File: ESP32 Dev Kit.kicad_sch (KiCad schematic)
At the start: 22 parts, among them J1 USB_B_Micro, Q1 2N2222, Q2 2N2222, SW1 SW_Push, SW2 SW_Push, U1 AMS1117-3.3, U2 CH340C

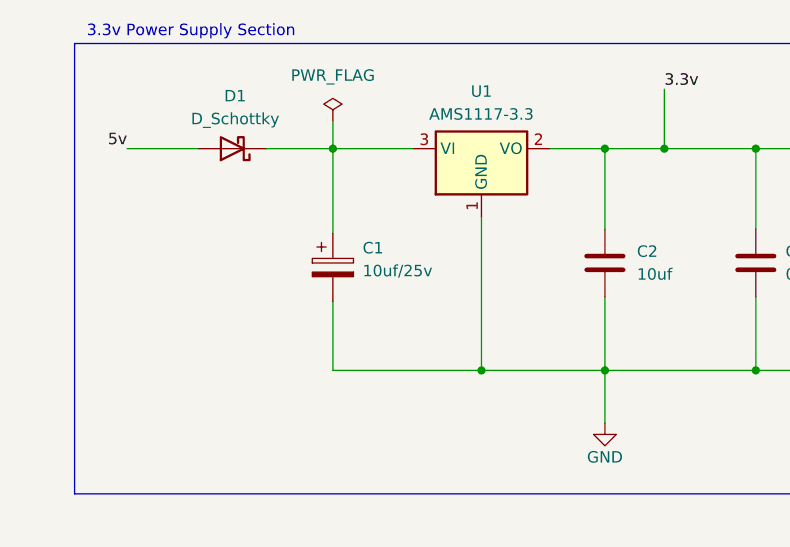
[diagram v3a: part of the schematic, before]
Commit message: Added Footprints to the Symbols
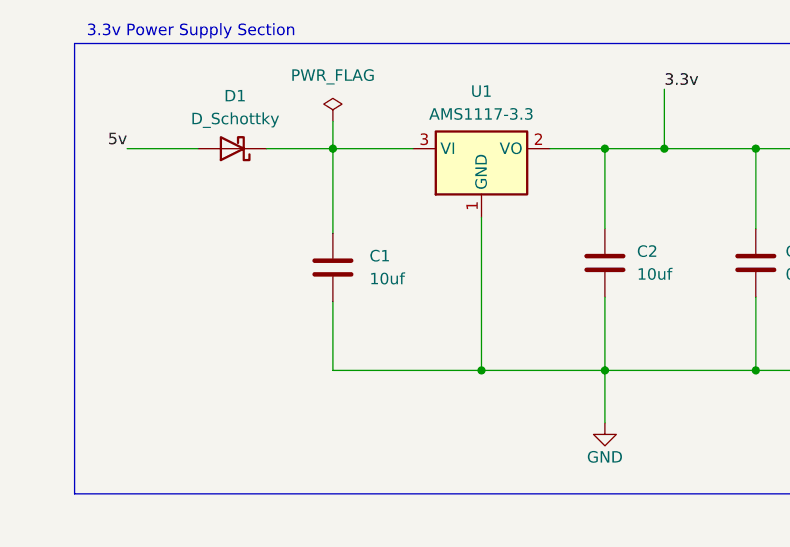
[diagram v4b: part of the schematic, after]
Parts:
- removed C1: 10uf/25v, symbol Device:C_Polarized
- added C1: 10uf, Capacitor_SMD:C_0805_2012Metric_Pad1.18x1.45mm_HandSolder, symbol Device:C
- C2, C3, C4, C5, C6: footprint (none) -> Capacitor_SMD:C_0805_2012Metric_Pad1.18x1.45mm_HandSolder
- D1: footprint (none) -> Diode_SMD:D_SOD-123
- D2: footprint (none) -> LED_SMD:LED_0805_2012Metric_Pad1.15x1.40mm_HandSolder
- J1: footprint (none) -> Connector_USB:USB_Micro-B_Molex_47346-0001
- R1, R2, R3, R4, R5, R6: footprint (none) -> Resistor_SMD:R_0805_2012Metric_Pad1.20x1.40mm_HandSolder
- SW1, SW2: footprint (none) -> Button_Switch_SMD:SW_SPST_B3U-1000P
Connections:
- net GND: now also C1.2
- net at D1.1 (K), U1.3 (VI): now also C1.1
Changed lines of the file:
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@@
 			)
 		)
-		(property "Footprint" ""
+		(property "Footprint" "Capacitor_SMD:C_0805_2012Metric_Pad1.18x1.45mm_HandSolder"
 			(at 220.218 70.6628 0)
 			(effects
@@
 			)
 		)
-		(property "Footprint" ""
+		(property "Footprint" "Connector_USB:USB_Micro-B_Molex_47346-0001"
 			(at 190.754 121.666 0)
 			(effects
@@
 			)
 		)
-		(property "Footprint" ""
+		(property "Footprint" "Resistor_SMD:R_0805_2012Metric_Pad1.20x1.40mm_HandSolder"
 			(at 114.808 41.148 90)
 			(effects
@@
 			)
 		)
-		(property "Footprint" ""
+		(property "Footprint" "Diode_SMD:D_SOD-123"
 			(at 48.26 39.37 0)
 			(effects
@@
 			)
 		)
-		(property "Footprint" ""
+		(property "Footprint" "Capacitor_SMD:C_0805_2012Metric_Pad1.18x1.45mm_HandSolder"
 			(at 177.4952 141.224 0)
 			(effects
@@
 			)
 		)
-		(property "Footprint" ""
+		(property "Footprint" "Resistor_SMD:R_0805_2012Metric_Pad1.20x1.40mm_HandSolder"
 			(at 171.704 44.958 90)
 			(effects
@@
 			)
 		)
-		(property "Footprint" ""
+		(property "Footprint" "Capacitor_SMD:C_0805_2012Metric_Pad1.18x1.45mm_HandSolder"
 			(at 107.3912 55.88 0)
 			(effects
@@
 			)
 		)
-		(property "Footprint" ""
+		(property "Footprint" "Resistor_SMD:R_0805_2012Metric_Pad1.20x1.40mm_HandSolder"
 			(at 182.626 137.668 90)
 			(effects
@@
 			)
 		)
-		(property "Footprint" ""
+		(property "Footprint" "Capacitor_SMD:C_0805_2012Metric_Pad1.18x1.45mm_HandSolder"
 			(at 90.6272 55.88 0)
 			(effects
@@
 			)
 		)
-		(property "Footprint" ""
+		(property "Footprint" "Button_Switch_SMD:SW_SPST_B3U-1000P"
 			(at 192.532 38.1 0)
 			(effects
@@
 			)
 		)
-		(property "Footprint" ""
+		(property "Footprint" "Button_Switch_SMD:SW_SPST_B3U-1000P"
 			(at 250.444 37.846 0)
 			(effects
@@
 			)
 		)
-		(property "Footprint" ""
+		(property "Footprint" "Capacitor_SMD:C_0805_2012Metric_Pad1.18x1.45mm_HandSolder"
 			(at 215.0872 110.744 0)
 			(effects
@@
 	)
 	(symbol
-		(lib_id "Device:C_Polarized")
+		(lib_id "Device:C")
 		(at 59.436 52.578 0)
 		(unit 1)
@@
 		(fields_autoplaced yes)
 		(property "Reference" "C1"
-			(at 62.738 50.4189 0)
-			(effects
-				(font
-					(size 1.27 1.27)
-				)
-				(justify left)
-			)
-		)
-		(property "Value" "10uf/25v"
-			(at 62.738 52.9589 0)
-			(effects
-				(font
-					(size 1.27 1.27)
-				)
-				(justify left)
-			)
-		)
-		(property "Footprint" ""
+			(at 63.5 51.3079 0)
+			(effects
+				(font
+					(size 1.27 1.27)
+				)
+				(justify left)
+			)
+		)
+		(property "Value" "10uf"
+			(at 63.5 53.8479 0)
+			(effects
+				(font
+					(size 1.27 1.27)
+				)
+				(justify left)
+			)
+		)
+		(property "Footprint" "Capacitor_SMD:C_0805_2012Metric_Pad1.18x1.45mm_HandSolder"
 			(at 60.4012 56.388 0)
 			(effects
@@
 			)
 		)
-		(property "Description" "Polarized capacitor"
+		(property "Description" "Unpolarized capacitor"
 			(at 59.436 52.578 0)
 			(effects
@@
 			)
 		)
-		(pin "1"
-		)
 		(pin "2"
 		)
-		(instances
-			(project ""
+		(pin "1"
+		)
+		(instances
+			(project "ESP32 Dev Kit"
 				(path "/56a9cdb5-133f-4918-8bc1-4c774ad33a13"
 					(reference "C1")
@@
 			)
 		)
-		(property "Footprint" ""
+		(property "Footprint" "Resistor_SMD:R_0805_2012Metric_Pad1.20x1.40mm_HandSolder"
 			(at 229.362 44.704 90)
 			(effects
@@
 			)
 		)
-		(property "Footprint" ""
+		(property "Footprint" "LED_SMD:LED_0805_2012Metric_Pad1.15x1.40mm_HandSolder"
 			(at 124.714 52.07 0)
 			(effects
@@
 			)
 		)
-		(property "Footprint" ""
+		(property "Footprint" "Resistor_SMD:R_0805_2012Metric_Pad1.20x1.40mm_HandSolder"
 			(at 257.302 54.864 90)
 			(effects
@@
 			)
 		)
-		(property "Footprint" ""
+		(property "Footprint" "Resistor_SMD:R_0805_2012Metric_Pad1.20x1.40mm_HandSolder"
 			(at 199.39 53.34 90)
 			(effects

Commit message: Schematic and Footprints Revised
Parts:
- removed MOD1: ESP32-WROOM-32, digikey-footprints:ESP32-WROOM-32D, symbol dk_RF-Transceiver-Modules:ESP32-WROOM-32
- added U3: ESP32-WROOM-32, RF_Module:ESP32-WROOM-32, symbol RF_Module:ESP32-WROOM-32
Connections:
- net 3.3v: now also U3.2 (VDD)
- net Boot: now also U3.25 (IO0)
- net D12: now also U3.14 (IO12)
- net D13: now also U3.16 (IO13)
- net D14: now also U3.13 (IO14)
- net D15: now also U3.23 (IO15)
- net D18: now also U3.30 (IO18)
- net D19: now also U3.31 (IO19)
- net D2: now also U3.24 (IO2)
- net D21: now also U3.33 (IO21)
- net D22: now also U3.36 (IO22)
- net D23: now also U3.37 (IO23)
- net D25: now also U3.10 (IO25)
- net D26: now also U3.11 (IO26)
- net D27: now also U3.12 (IO27)
- net D32: now also U3.8 (IO32)
- net D33: now also U3.9 (IO33)
- net D34: now also U3.6 (IO34)
- net D35: now also U3.7 (IO35)
- net D4: now also U3.26 (IO4)
- net D5: now also U3.29 (IO5)
- net EN: now also U3.3 (EN)
- net GND: now also U3.1 (GND), U3.15 (GND), U3.38 (GND), U3.39 (GND)
- net RX0: now also U3.34 (RXD0/IO3)
- net RX2: now also U3.27 (IO16)
- net TX0: now also U3.35 (TXD0/IO1)
- net TX2: now also U3.28 (IO17)
- net VN: now also U3.5 (SENSOR_VN)
- net VP: now also U3.4 (SENSOR_VP)

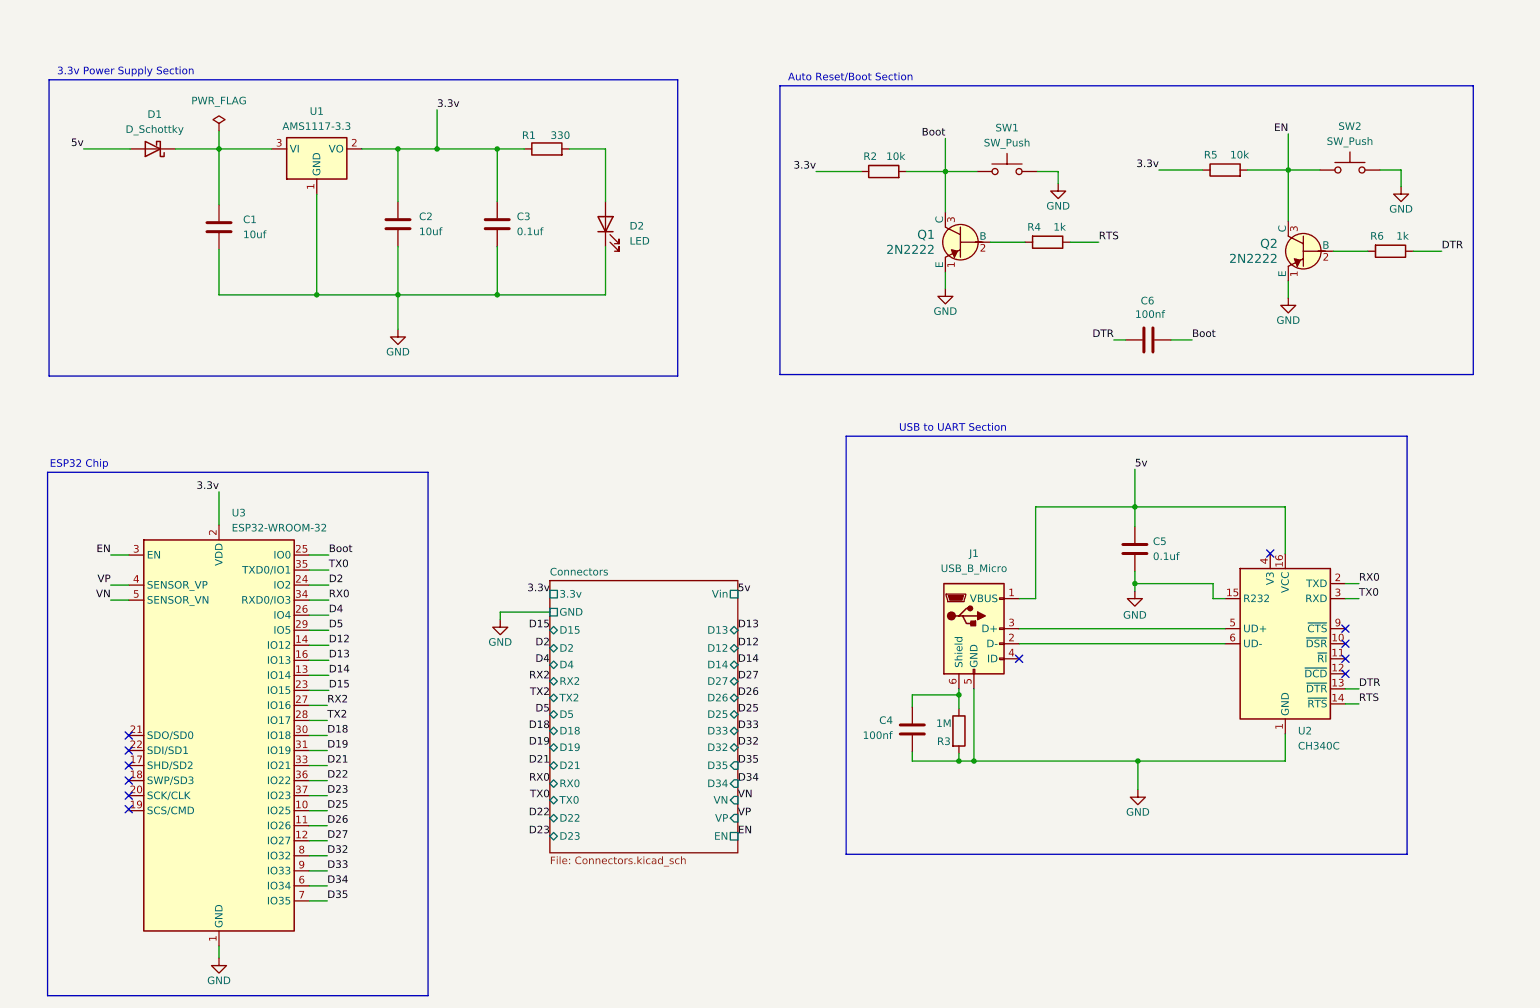
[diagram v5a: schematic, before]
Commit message: Footprints placed & Revised
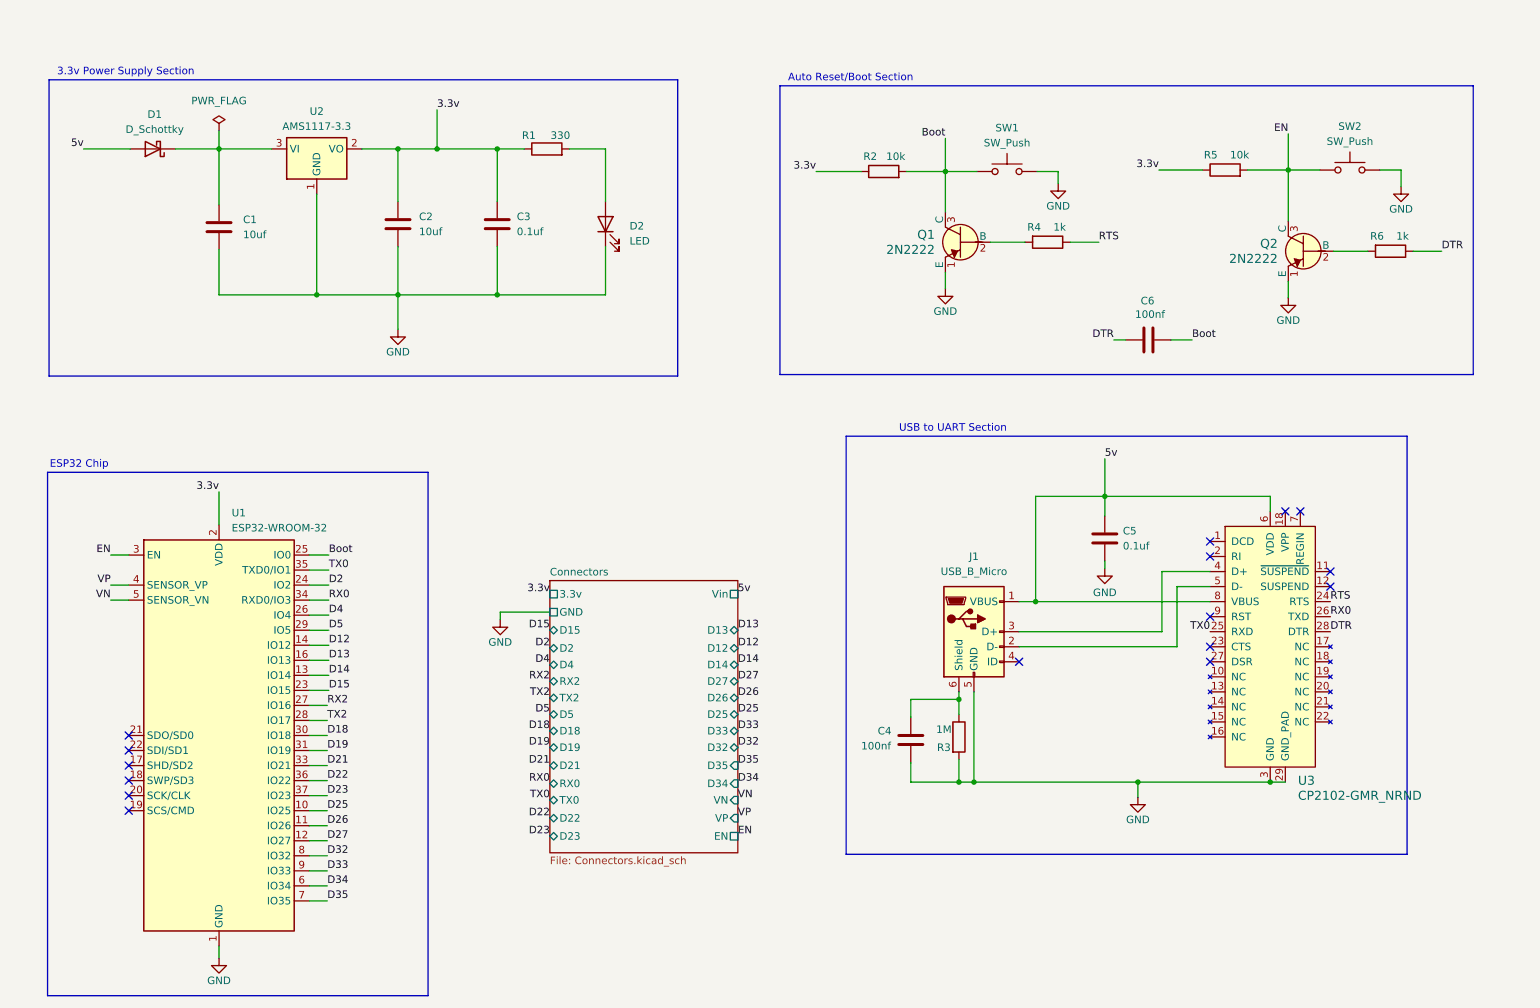
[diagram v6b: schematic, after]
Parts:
- removed U2: CH340C, SparkFun-Semiconductor-Standard:SO-16, symbol SparkFun-IC-Comm:CH340C
- added U3: CP2102-GMR_NRND, digikey-footprints:VFQFN-28-1EP_5x5mm, symbol dk_Interface-Controllers:CP2102-GMR_NRND
- Q1, Q2: footprint digikey-footprints:TO-18-3 -> Package_TO_SOT_SMD:SOT-23
- renumbered U3 to U1, U1 to U2
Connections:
- net 5v: now also U3.6 (VDD), U3.8 (VBUS)
- net DTR: now also U3.28 (DTR)
- net GND: now also U3.29 (GND_PAD), U3.3 (GND)
- net RTS: now also U3.24 (RTS)
- net RX0: now also U3.26 (TXD)
- net TX0: now also U3.25 (RXD)
- net at J1.2 (D-): now also U3.5 (D-)
- net at J1.3 (D+): now also U3.4 (D+)
- no-connect marks 12 -> 16
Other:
- moved on the sheet: C4, C5, J1, R3
